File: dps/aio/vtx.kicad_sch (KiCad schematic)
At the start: 16 parts, among them J201 HD VTX, J202 LD06, U201 LMR51430YFDDCR, U202 INA226AIDGSR

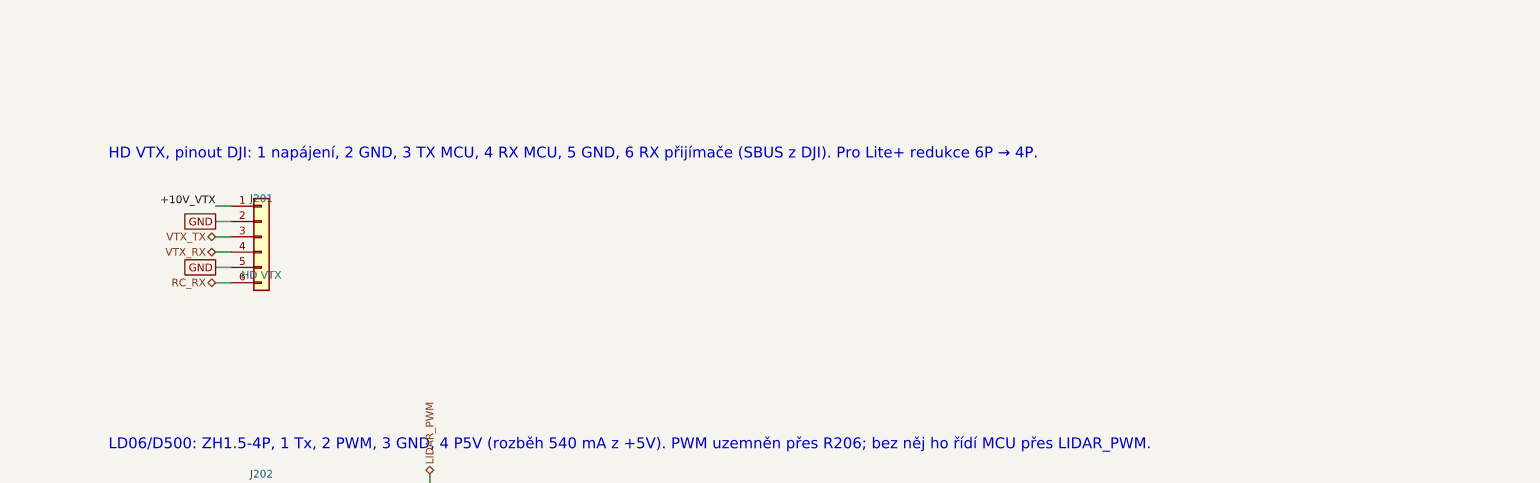
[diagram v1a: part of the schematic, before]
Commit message: feat: add the peripheral connectors to the AIO, from the makers' pinouts
- J303 SH1.0-6P for the WS-M181 GPS in the order printed on the module
  (TX RX GND 5V SCL SDA), with 4.7k pull-ups on the external I2C for its
  IST8310; J304 SH1.0-4P for the MTF-02P (GND 5V Rx Tx, robofusion; MicoAir
  draws the same signals from the other end). Neither maker says where pin 1
  is, so both are marked to check with a meter before first power.
- Pads for the XR1 Nano (it has castellated pads, no connector), UART1 and
  UART8, and the free PWM5, 7, 9, 10, 11.
- J201 pin 6 (SBUS from a DJI unit) now reaches USART6 RX only through JP202,
  open by default: the XR1's TX drives that line, and MicoAir's hard link
  would put two transmitters on it.
- NAVRH, README, hwdef comment and web texts follow; ERC still 18, explained.

Co-Authored-By: Claude Opus 5.5 <noreply@anthropic.com>
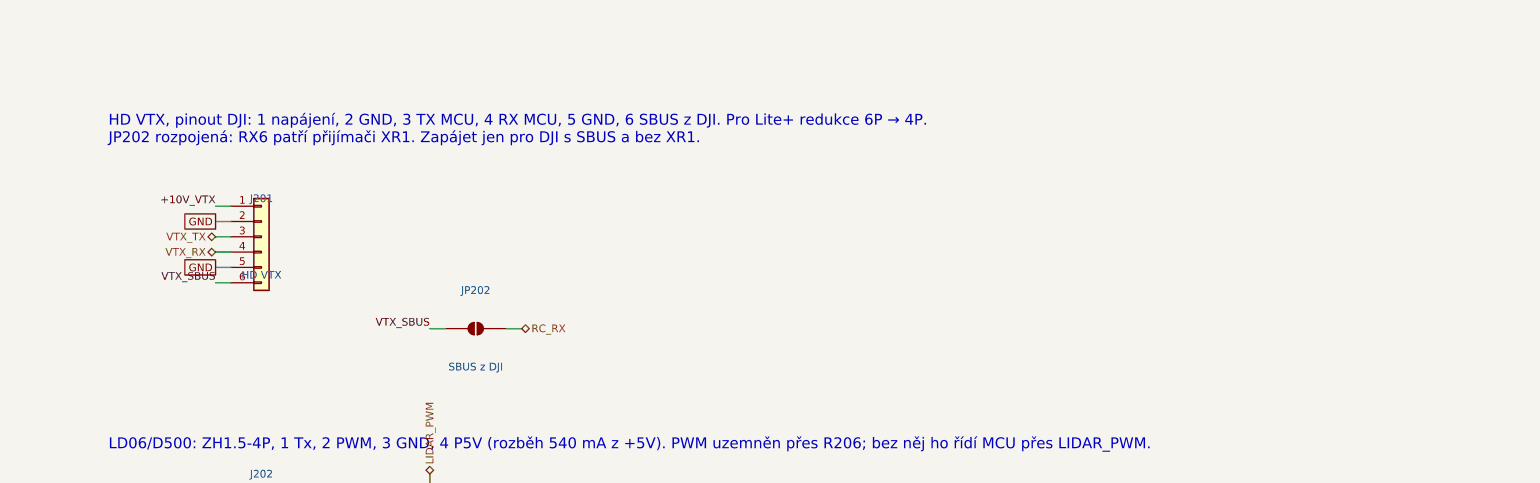
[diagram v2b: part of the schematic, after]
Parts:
- added JP202: SBUS z DJI, Jumper:SolderJumper-2_P1.3mm_Open_Pad1.0x1.5mm, symbol Jumper:SolderJumper_2_Open
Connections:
- net RC_RX: now also JP202.2 (B); no longer J201.6 (Pin_6)
- new net VTX_SBUS: J201.6 (Pin_6), JP202.1 (A)
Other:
- note added: "HD VTX, pinout DJI: 1 napájení, 2 GND, 3 TX MCU, 4 RX MCU, 5 GND, 6 SBUS z DJI. Pro Lite+ redukce 6P → 4P. JP202 rozpojená: RX6 patří přijímači XR1. Zapájet jen pro DJI s SBUS a bez XR1."
- note removed: "HD VTX, pinout DJI: 1 napájení, 2 GND, 3 TX MCU, 4 RX MCU, 5 GND, 6 RX přijímače (SBUS z DJI). Pro Lite+ redukce 6P → 4P."
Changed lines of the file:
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@@
 		)
 	)
-	(hierarchical_label "RC_RX"
-		(shape bidirectional)
+	(label "VTX_SBUS"
 		(at 195.58 124.46 180)
 		(effects
@@
 				(size 1.27 1.27)
 			)
-			(justify right)
+			(justify right bottom)
 		)
 	)
@@
 	)
 	(symbol
+		(lib_id "Jumper:SolderJumper_2_Open")
+		(at 238.76 132.08 0)
+		(unit 1)
+		(body_style 1)
+		(exclude_from_sim no)
+		(in_bom yes)
+		(on_board yes)
+		(in_pos_files yes)
+		(dnp no)
+		(property "Reference" "JP202"
+			(at 238.76 125.73 0)
+			(show_name no)
+			(do_not_autoplace no)
+			(effects
+				(font
+					(size 1.27 1.27)
+				)
+			)
+		)
+		(property "Value" "SBUS z DJI"
+			(at 238.76 138.43 0)
+			(show_name no)
+			(do_not_autoplace no)
+			(effects
+				(font
+					(size 1.27 1.27)
+				)
+			)
+		)
+		(property "Footprint" "Jumper:SolderJumper-2_P1.3mm_Open_Pad1.0x1.5mm"
+			(at 238.76 132.08 0)
+			(hide yes)
+			(show_name no)
+			(do_not_autoplace no)
+			(effects
+				(font
+					(size 1.27 1.27)
+				)
+			)
+		)
+		(property "Datasheet" ""
+			(at 238.76 132.08 0)
+			(hide yes)
+			(show_name no)
+			(do_not_autoplace no)
+			(effects
+				(font
+					(size 1.27 1.27)
+				)
+			)
+		)
+		(pin "1"
+		)
+		(pin "2"
+		)
+		(instances
+			(project "aio"
+				(path "/fb88b6f9-ee39-4640-a9d4-04a17ceeac64/1052a4a9-9195-58b6-8061-975967a9ab78"
+					(reference "JP202")
+					(unit 1)
+				)
+			)
+		)
+	)
+	(wire
+		(pts
+			(xy 233.68 132.08)
+			(xy 231.14 132.08)
+		)
+		(stroke
+			(width 0)
+			(type default)
+		)
+	)
+	(label "VTX_SBUS"
+		(at 231.14 132.08 180)
+		(effects
+			(font
+				(size 1.27 1.27)
+			)
+			(justify right bottom)
+		)
+	)
+	(wire
+		(pts
+			(xy 243.84 132.08)
+			(xy 246.38 132.08)
+		)
+		(stroke
+			(width 0)
+			(type default)
+		)
+	)
+	(hierarchical_label "RC_RX"
+		(shape bidirectional)
+		(at 246.38 132.08 0)
+		(effects
+			(font
+				(size 1.27 1.27)
+			)
+			(justify left)
+		)
+	)
+	(symbol
 		(lib_id "power:PWR_FLAG")
 		(at 50.8 190.5 0)
@@
 		)
 	)
-	(text "HD VTX, pinout DJI: 1 napájení, 2 GND, 3 TX MCU, 4 RX MCU, 5 GND, 6 RX přijímače (SBUS z DJI). Pro Lite+ redukce 6P → 4P."
-		(exclude_from_sim no)
-		(at 177.8 104.14 0)
-		(effects
-			(font
+	(text "HD VTX, pinout DJI: 1 napájení, 2 GND, 3 TX MCU, 4 RX MCU, 5 GND, 6 SBUS z DJI. Pro Lite+ redukce 6P → 4P.\nJP202 rozpojená: RX6 patří přijímači XR1. Zapájet jen pro DJI s SBUS a bez XR1."
+		(exclude_from_sim no)
+		(at 177.8 101.6 0)
+		(effects
+			(font

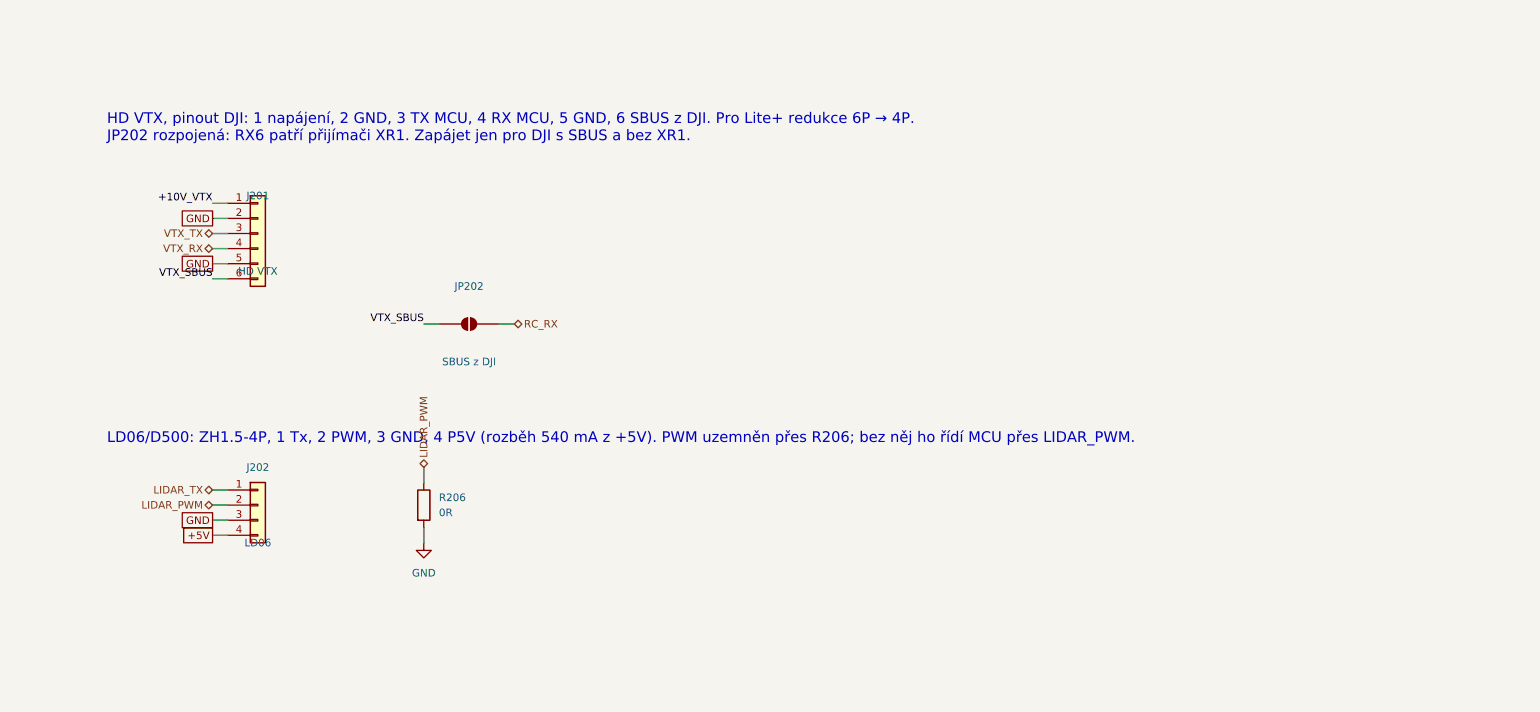
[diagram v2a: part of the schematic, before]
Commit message: feat: give the AIO MicoAir743-AIO's peripheral connectors
- J303 GPS (UART3 + I2C1), J304 UART4 and new J305 UART1 + UART6, SH1.0
  side entry, in MicoAir's order with pin 1 = GND (ArduPilot's README for the
  board puts pin 1 of the DJI connector at 12 V, the last row of its tables),
  so cables from a MicoAir fit. J305 replaces the XR1 and UART1 pads.
- The LD06 goes to pads (TP201 Tx, TP202 PWM, 5V/GND on TP320/TP321) as on
  MicoAir: the ZH1.5 connector needed 86 mm2 in one piece.
- Symbols and sheets now get UUIDs from their names, so adding or removing a
  part no longer shifts the others and breaks their link to the board.
- Placement: J304 fits on the back right edge as on MicoAir. J303 and J305 do
  not: every spot for a 6-pin SH (side 9.8 x 6.6 or vertical 9.8 x 5.2 mm)
  hits the ESC and power parts kept from OpenAIO, so they stay off the board.

Co-Authored-By: Claude Opus 5.5 <noreply@anthropic.com>
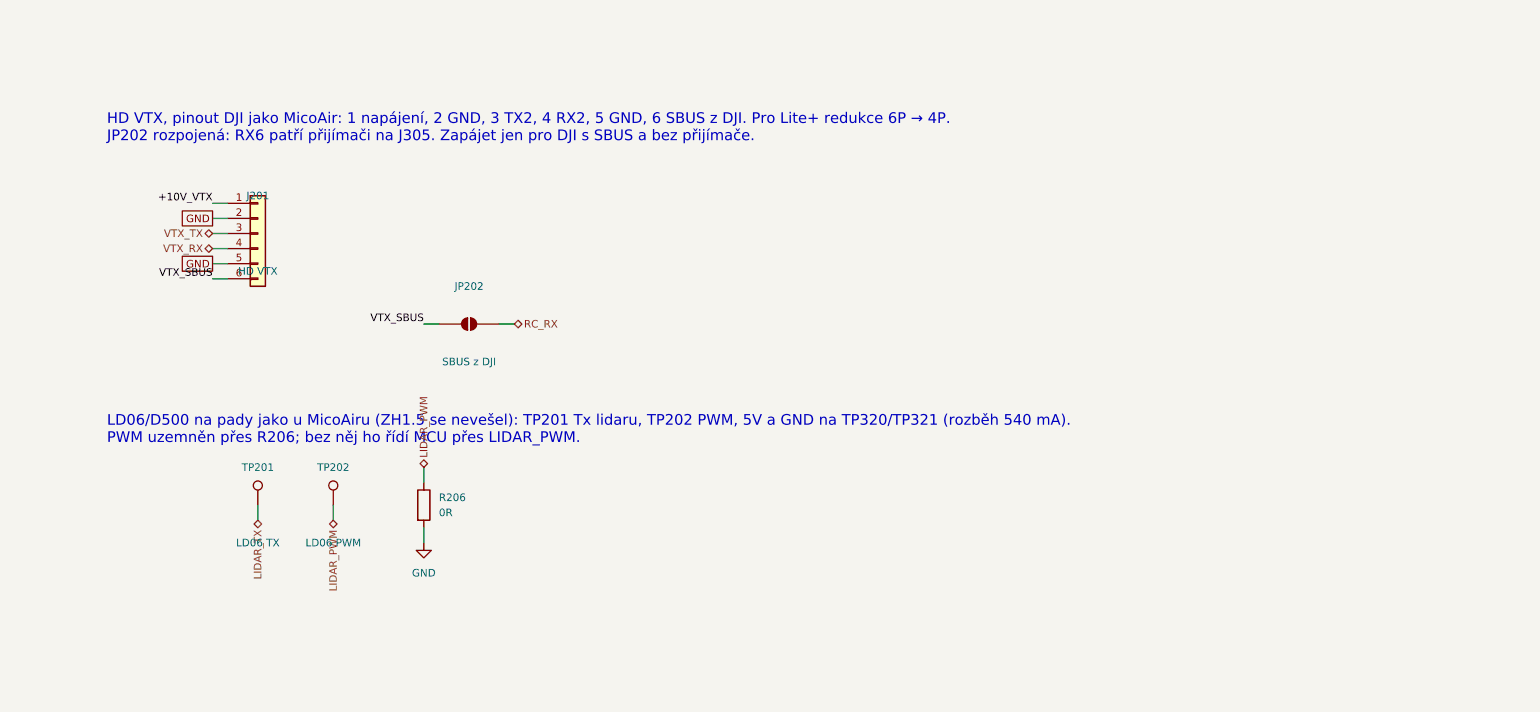
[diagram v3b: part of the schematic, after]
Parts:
- removed J202: LD06, Connector_JST:JST_ZH_S4B-ZR-SM4A-TF_1x04-1MP_P1.50mm_Horizontal, symbol Connector_Generic:Conn_01x04
- added TP201: LD06 TX, lib:TestPoint_Pad_D1.0mm, symbol lib:TestPoint
- added TP202: LD06 PWM, lib:TestPoint_Pad_D1.0mm, symbol lib:TestPoint
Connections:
- net LIDAR_PWM: now also TP202.1
- net LIDAR_TX: now also TP201.1
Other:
- note added: "HD VTX, pinout DJI jako MicoAir: 1 napájení, 2 GND, 3 TX2, 4 RX2, 5 GND, 6 SBUS z DJI. Pro Lite+ redukce 6P → 4P. JP202 rozpojená: RX6 patří přijímači na J305. Zapájet jen pro DJI s SBUS a bez přijímače."
- note added: "LD06/D500 na pady jako u MicoAiru (ZH1.5 se nevešel): TP201 Tx lidaru, TP202 PWM, 5V a GND na TP320/TP321 (rozběh 540 mA). PWM uzemněn přes R206; bez něj ho řídí MCU přes LIDAR_PWM."
- note removed: "HD VTX, pinout DJI: 1 napájení, 2 GND, 3 TX MCU, 4 RX MCU, 5 GND, 6 SBUS z DJI. Pro Lite+ redukce 6P → 4P. JP202 rozpojená: RX6 patří přijímači XR1. Zapájet jen pro DJI s SBUS a bez XR1."
- note removed: "LD06/D500: ZH1.5-4P, 1 Tx, 2 PWM, 3 GND, 4 P5V (rozběh 540 mA z +5V). PWM uzemněn přes R206; bez něj ho řídí MCU přes LIDAR_PWM."

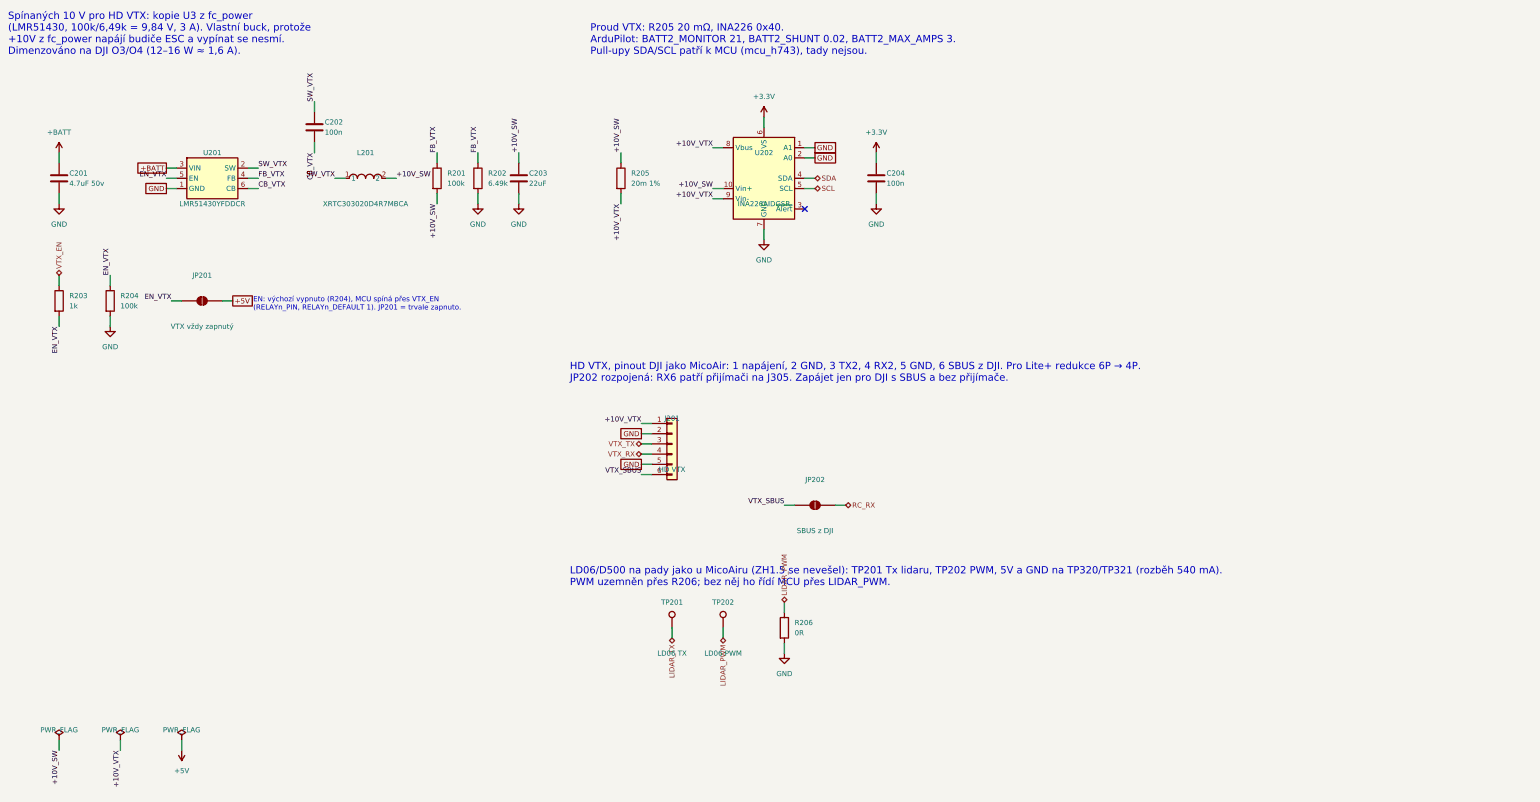
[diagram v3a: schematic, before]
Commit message: feat: put all four MicoAir connectors on the AIO's edge and place it without the INA226
- The edge search found four spots no kept OpenAIO part blocks, so the ESCs
  stay as they are: J201 VTX front bottom, J303 GPS front right below motor 4,
  J305 UART1+UART6 back right, J304 UART4 back bottom. Motor pads are front
  only and the battery pads take the top edge, hence not MicoAir's places.
- Pads as on MicoAir: new lib:Pad_1.0x1.4mm (courtyard 1.2 x 1.6) instead of
  1 mm round test points with a 2 x 2 courtyard.
- Dropped for room, none of them on MicoAir: the VTX INA226 with its shunt,
  JP201 and the buzzer diode; Q301 is OpenAIO's AP1606 in DFN 1.0 x 0.6
  instead of an AO3400A in SOT-23. BATT2 defaults go; firmware rebuilt.
- Placement now treats pads, holes on both sides and the outer-layer copper
  of nets no new part uses (ESC inside, +BATT, the CSA+ via field) as
  obstacles, in 1 mm cells. vycisti_med.py removes the dangling RP2354
  leftovers and copper the new parts land on, never CSA+ or +BATT; the
  updater swaps changed footprints and sets sheet names.
- U303 (BMI088) and U201 (VTX buck) do not fit: no 3.3 x 3.3 mm is left on
  either side. DRC: 163 unconnected, otherwise OpenAIO's own warnings.

Co-Authored-By: Claude Opus 5.5 <noreply@anthropic.com>
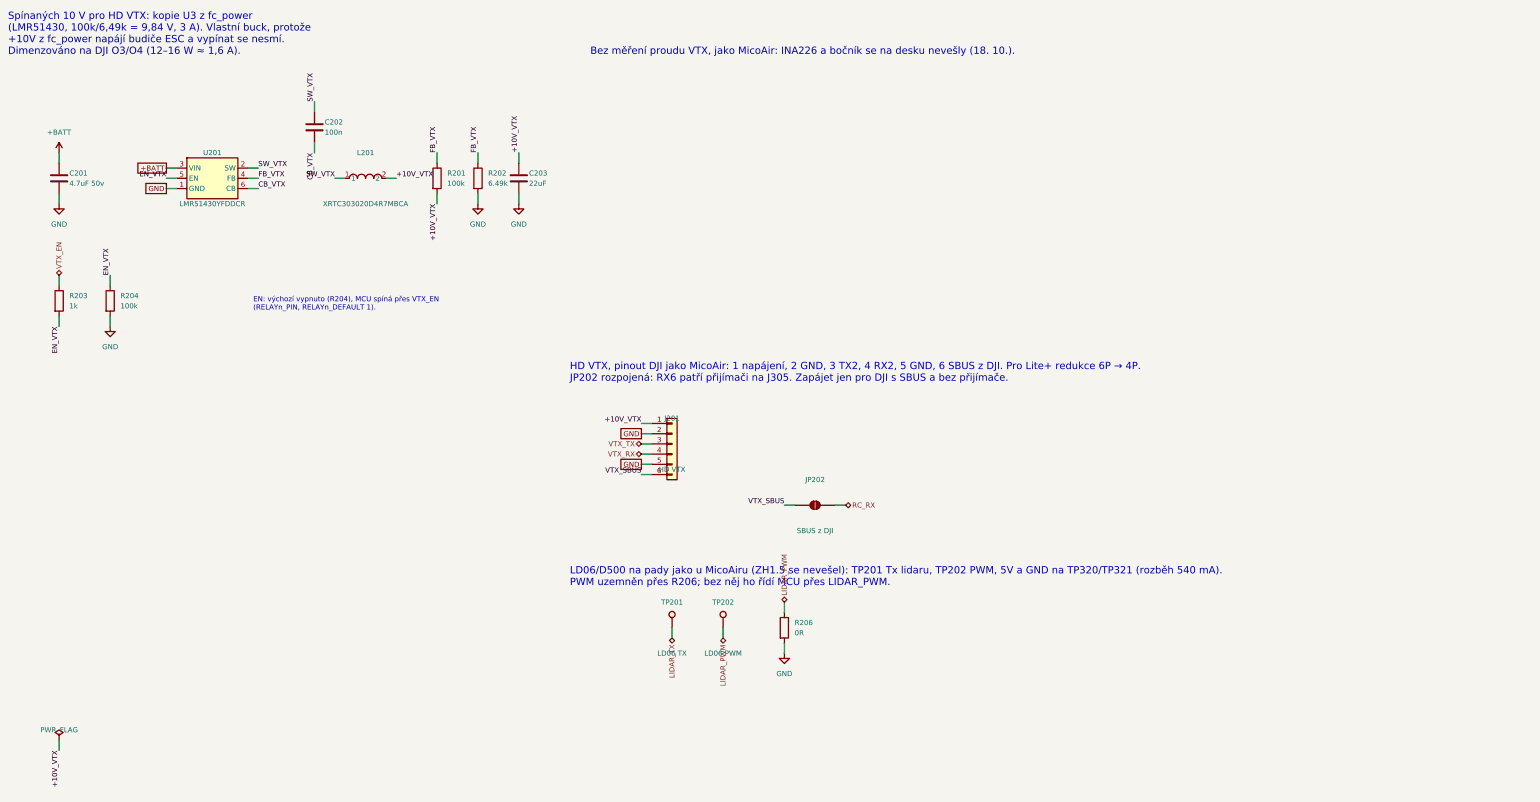
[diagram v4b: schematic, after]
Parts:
- removed C204: 100n, lib:C_0201_0603Metric, symbol lib:C
- removed JP201: VTX vždy zapnutý, Jumper:SolderJumper-2_P1.3mm_Open_Pad1.0x1.5mm, symbol Jumper:SolderJumper_2_Open
- removed R205: 20m 1%, Resistor_SMD:R_0805_2012Metric, symbol lib:R
- removed U202: INA226AIDGSR, Package_SO:TSSOP-10_3x3mm_P0.5mm, symbol Sensor_Energy:INA226
- TP201, TP202: footprint lib:TestPoint_Pad_D1.0mm -> lib:Pad_1.0x1.4mm
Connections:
- net +10V_SW is gone; now on net +10V_VTX: C203.1, L201.2, R201.2
- no-connect marks 1 -> 0
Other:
- note added: "Bez měření proudu VTX, jako MicoAir: INA226 a bočník se na desku nevešly (18. 10.)."
- note added: "EN: výchozí vypnuto (R204), MCU spíná přes VTX_EN (RELAYn_PIN, RELAYn_DEFAULT 1)."
- note removed: "EN: výchozí vypnuto (R204), MCU spíná přes VTX_EN (RELAYn_PIN, RELAYn_DEFAULT 1). JP201 = trvale zapnuto."
- note removed: "Proud VTX: R205 20 mΩ, INA226 0x40. ArduPilot: BATT2_MONITOR 21, BATT2_SHUNT 0.02, BATT2_MAX_AMPS 3. Pull-upy SDA/SCL patří k MCU (mcu_h743), tady nejsou."
